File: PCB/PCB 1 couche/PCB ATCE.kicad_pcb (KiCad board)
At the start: 2 copper layers, 41.7 x 34.6 mm, 29 parts, among them J1 USB_OTG, J2 Conn_Coaxial, SW1 SW_Push, SW2 SW_Push, Y1 16MHz

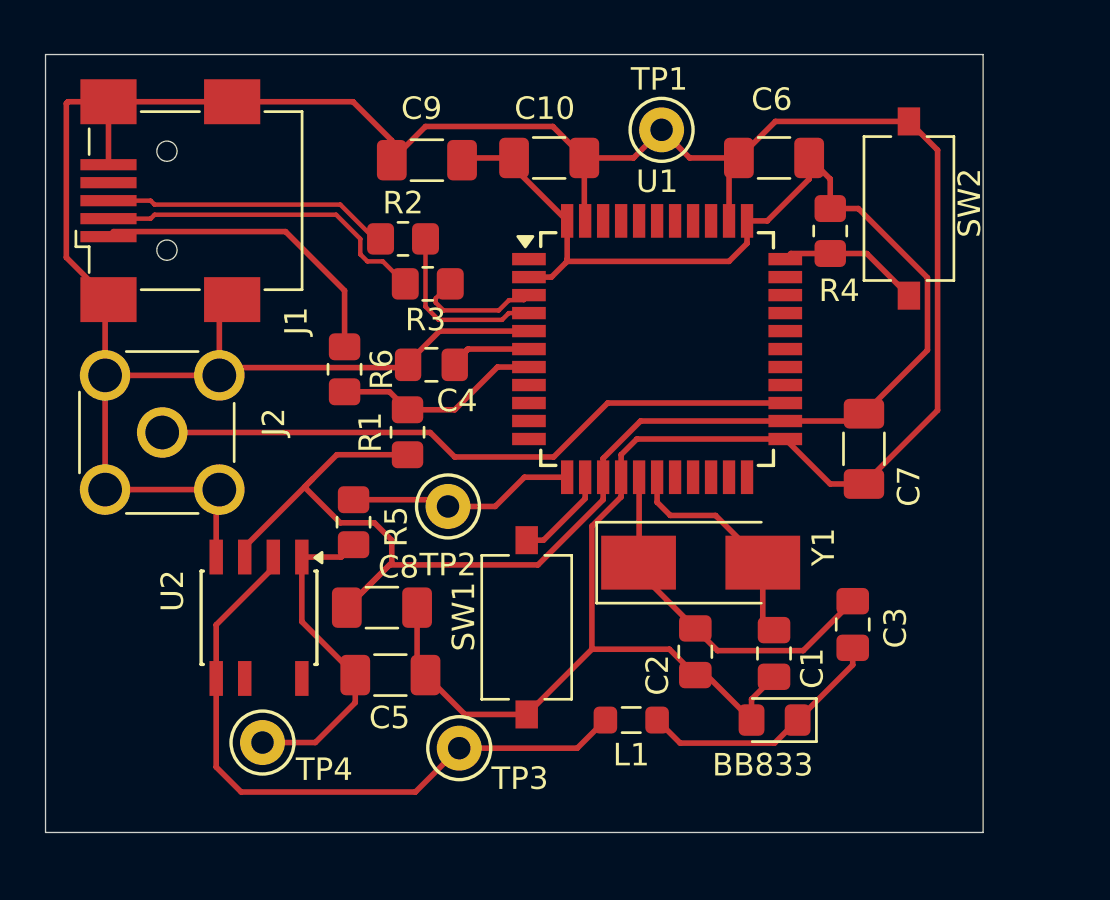
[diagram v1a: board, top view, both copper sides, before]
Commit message: modification pcb une couche suite au changement du pwm
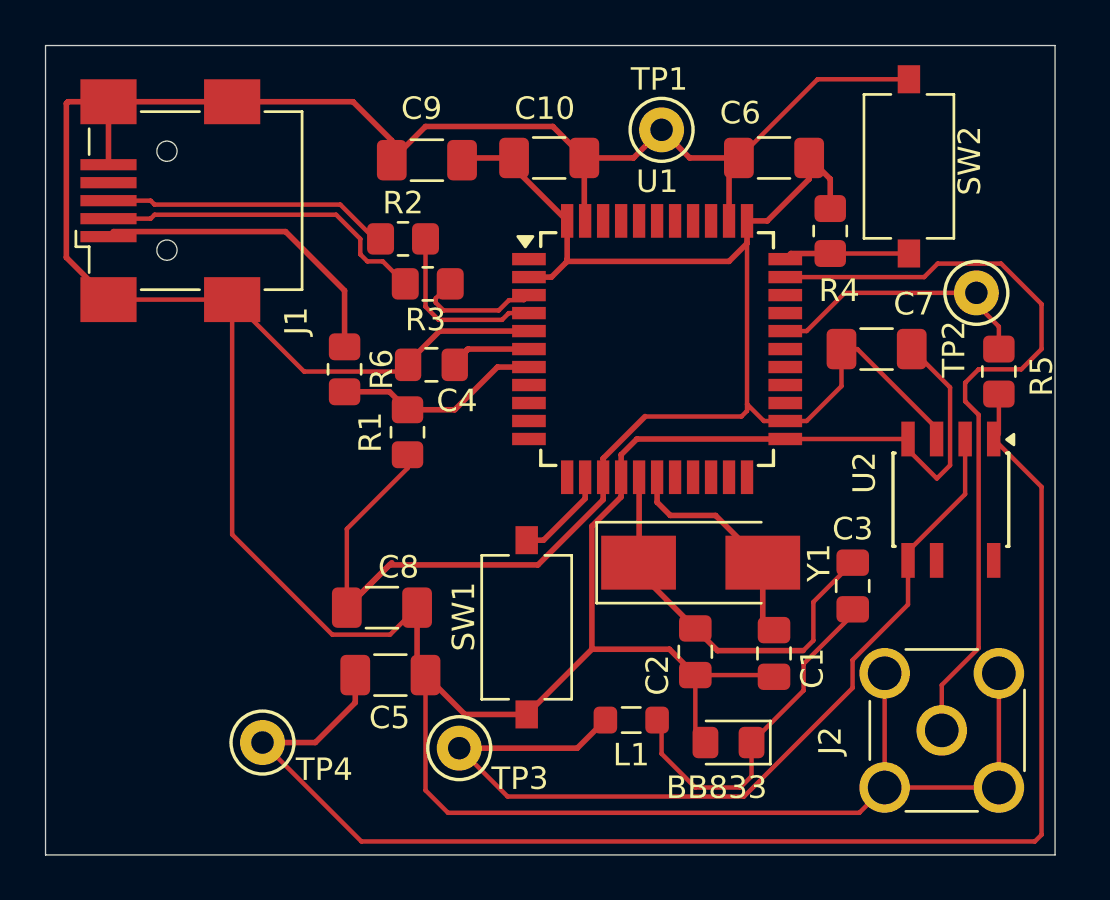
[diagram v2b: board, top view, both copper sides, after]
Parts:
- moved J2 37.1 mm to (151.0, 106.5), turned to -90 degrees
- moved U2 31.2 mm to (151.4, 96.2)
- moved R5 29.5 mm to (153.5, 90.5)
- moved TP2 25.3 mm to (152.5, 87.0)
- moved C7 4.47 mm to (148.1, 89.5), turned to 0 degrees
- moved BB833 2.28 mm to (141.5, 107.0)
- moved SW2 1.88 mm to (149.5, 81.4)
- moved C3 1.71 mm to (147.0, 100.0)
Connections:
- R5 pad 1: Net-(U1-(OC0A/OC1C/~{RTS}/PCINT7)PB7) -> Net-(U1-(ADC12/OC1A/~{OC4B}/PCINT5)PB5)
- TP2 pad 1: Net-(U1-(OC0A/OC1C/~{RTS}/PCINT7)PB7) -> Net-(U1-(ADC12/OC1A/~{OC4B}/PCINT5)PB5)
- U1 pad 12: Net-(U1-(OC0A/OC1C/~{RTS}/PCINT7)PB7) -> unconnected-(U1-(OC0A/OC1C/~{RTS}/PCINT7)PB7-Pad12)
- U1 pad 25: Net-(J2-In) -> unconnected-(U1-(ICP1/ADC8)PD4-Pad25)
- U1 pad 29: unconnected-(U1-(ADC12/OC1A/~{OC4B}/PCINT5)PB5-Pad29) -> Net-(U1-(ADC12/OC1A/~{OC4B}/PCINT5)PB5)
- U1 pad 32: unconnected-(U1-(ICP3/CLK0/OC4A)PC7-Pad32) -> Net-(J2-In)
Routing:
- net Net-(U2-+): track 14.8 -> 63.3 mm
- net GND: track 162.8 -> 202.5 mm
- net Net-(U1-(ADC12/OC1A/~{OC4B}/PCINT5)PB5): track 0.00 -> 12.1 mm
- net Net-(U2--): track 29.5 -> 40.5 mm
- net Net-(U1-(OC0A/OC1C/~{RTS}/PCINT7)PB7): track 10.2 -> 0.00 mm
- net Net-(J2-In): track 29.2 -> 34.8 mm
- net +5V: track 85.9 -> 81.0 mm
- net Net-(BB833-K): track 11.3 -> 15.7 mm
- net Net-(U1-XTAL2): track 16.1 -> 17.8 mm
- net Net-(U1-(~{HWB})PE2): track 6.38 -> 5.60 mm
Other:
- board size 41.7 x 34.6 mm -> 44.9 x 36 mm

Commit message: modification pcb (empreinte test point + routage nouveau pwm)
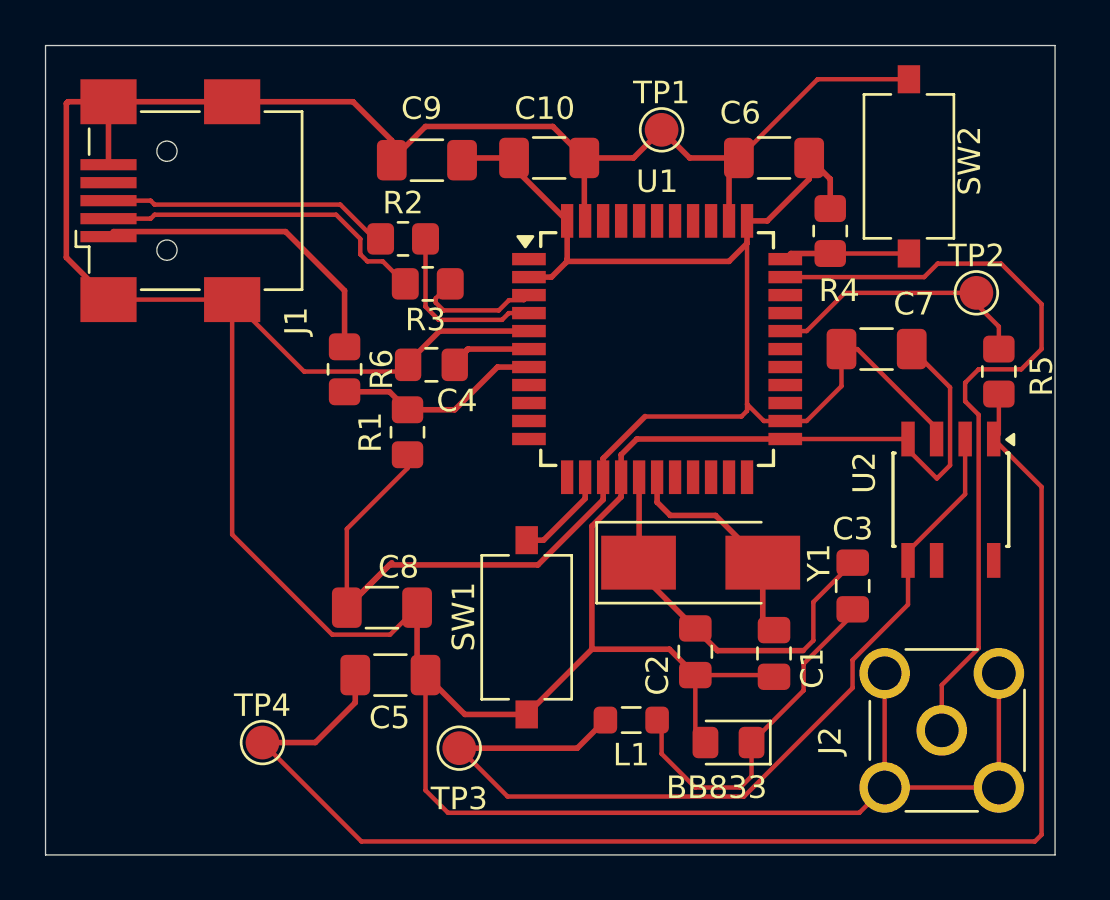
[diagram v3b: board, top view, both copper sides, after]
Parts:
- TP1, TP2, TP3, TP4: footprint TestPoint:TestPoint_Keystone_5000-5004_Miniature -> TestPoint:TestPoint_Pad_D1.5mm
